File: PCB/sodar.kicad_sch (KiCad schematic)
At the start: 69 parts, among them J1 Conn_02x12_Counter_Clockwise, J2 Screw_Terminal_01x02, U1 TC78H621FNG, U10 TC78H621FNG, U2 TC78H621FNG, U3 TC78H621FNG, U4 TC78H621FNG, U5 TC78H621FNG, U6 TC78H621FNG, U7 TC78H621FNG, U8 TC78H621FNG, U9 TC78H621FNG

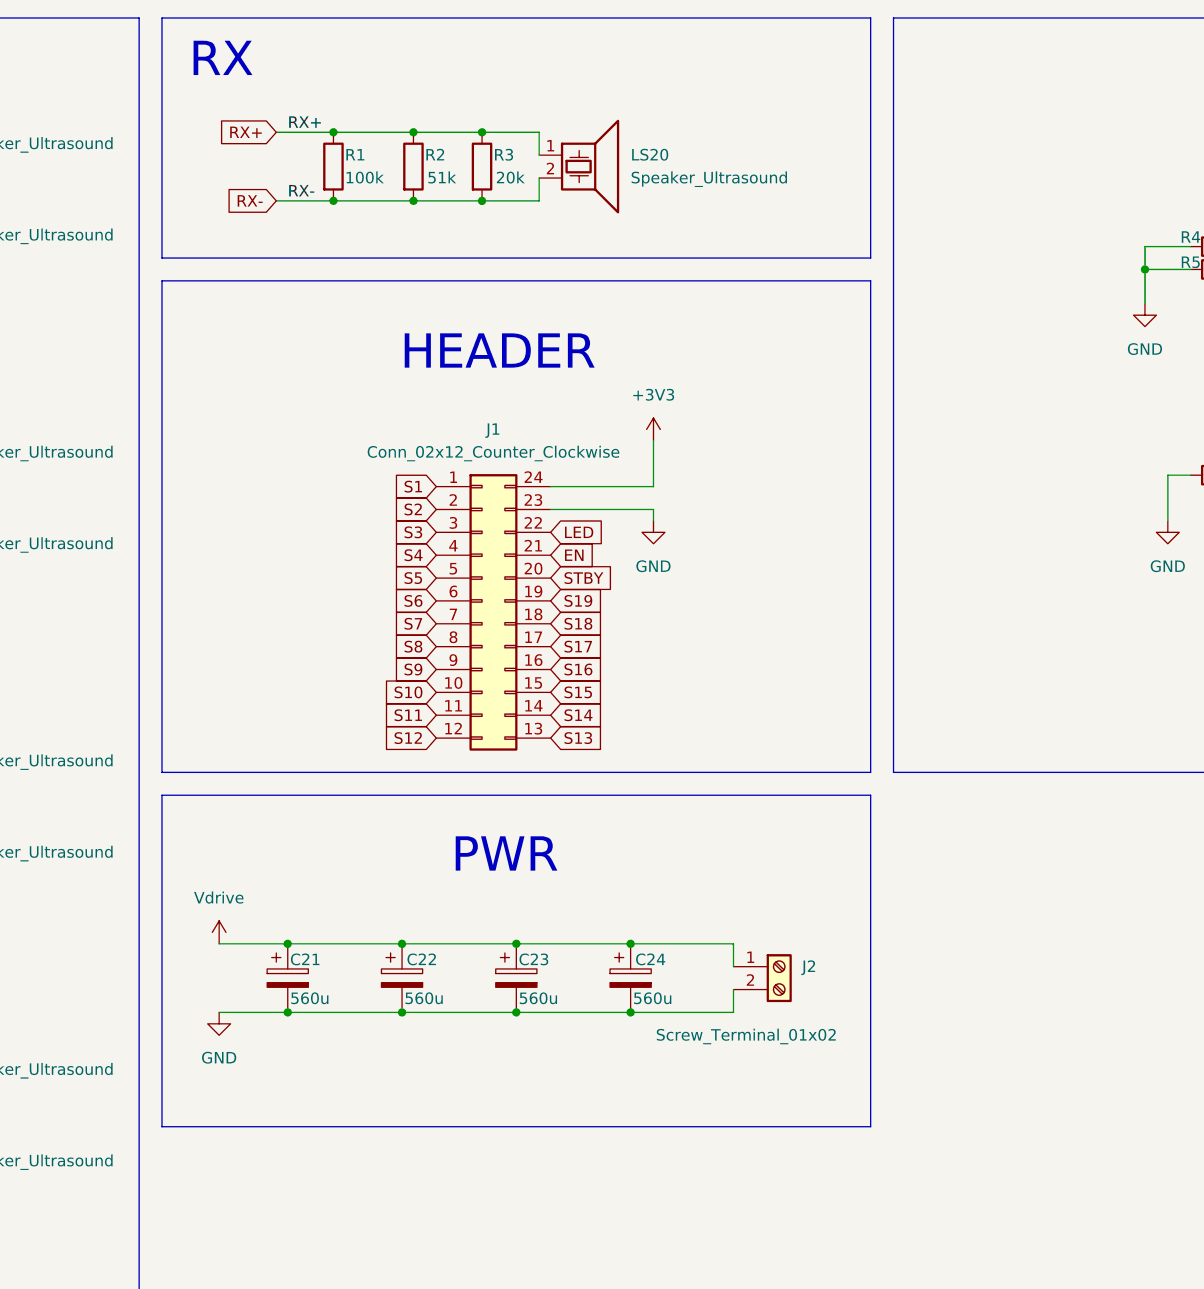
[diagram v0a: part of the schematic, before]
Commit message: Fixed receiver schematics
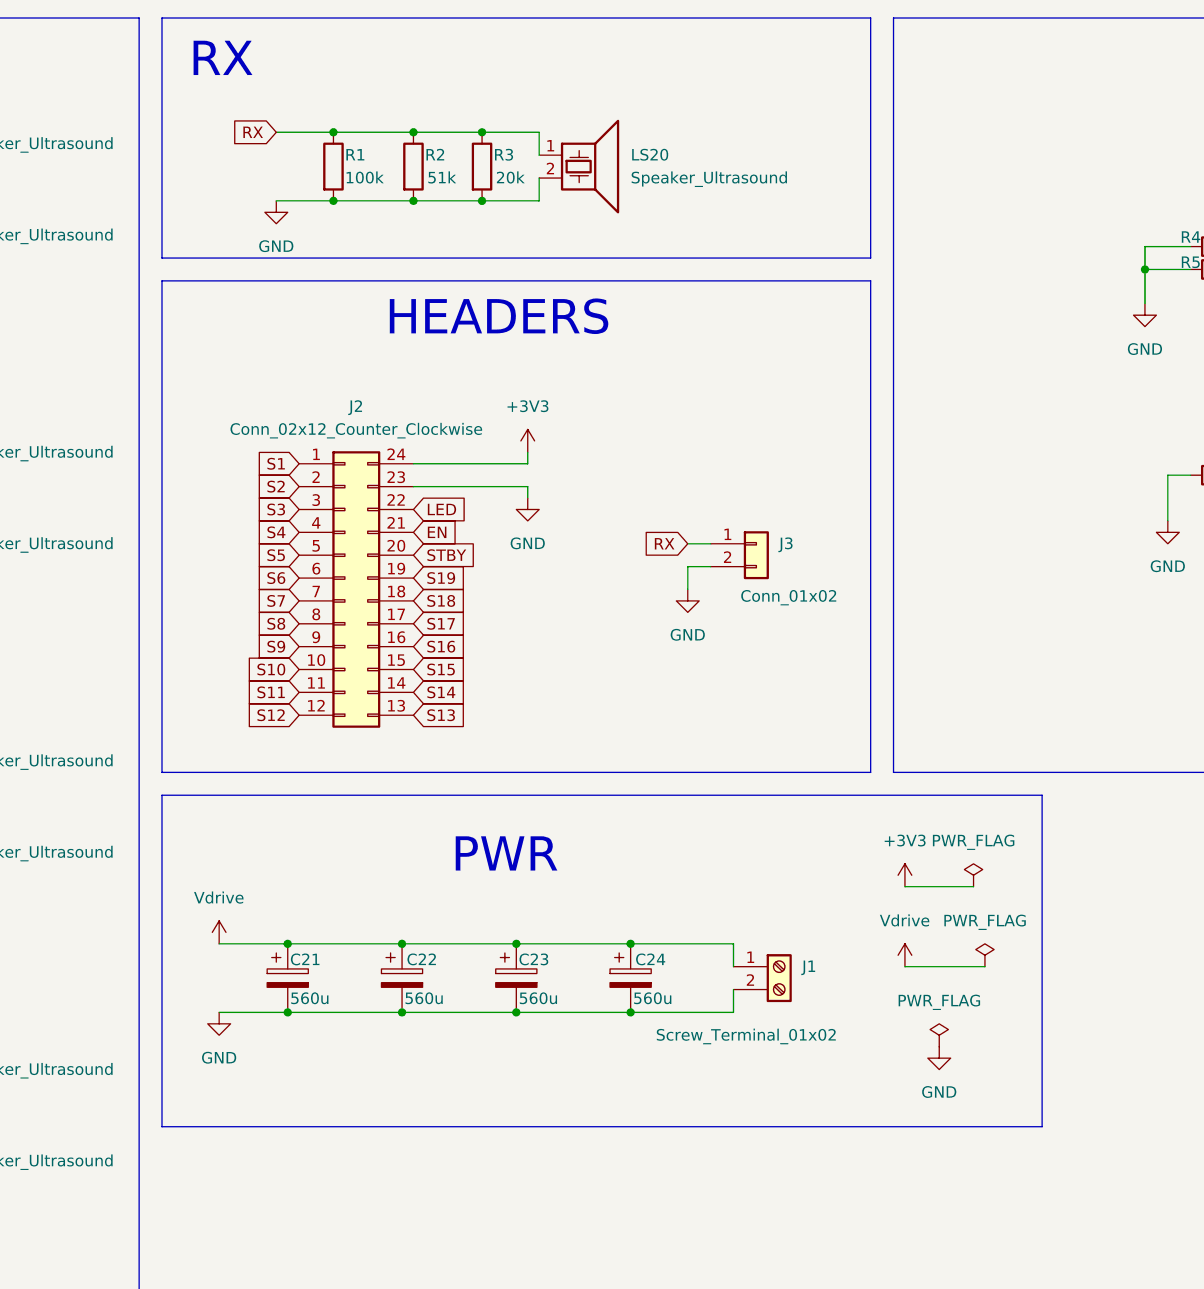
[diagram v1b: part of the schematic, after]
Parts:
- added J3: Conn_01x02, Connector_PinSocket_2.54mm:PinSocket_1x02_P2.54mm_Vertical, symbol Connector_Generic:Conn_01x02
- renumbered J2 to J1, J1 to J2
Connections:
- net RX- is gone; now on net GND: LS20.2, R1.2, R2.2, R3.2
- net GND: now also J3.2 (Pin_2)
- net RX+ renamed RX
- net RX: now also J3.1 (Pin_1)
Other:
- note added: "HEADERS"
- note removed: "HEADER"
- moved on the sheet: J2

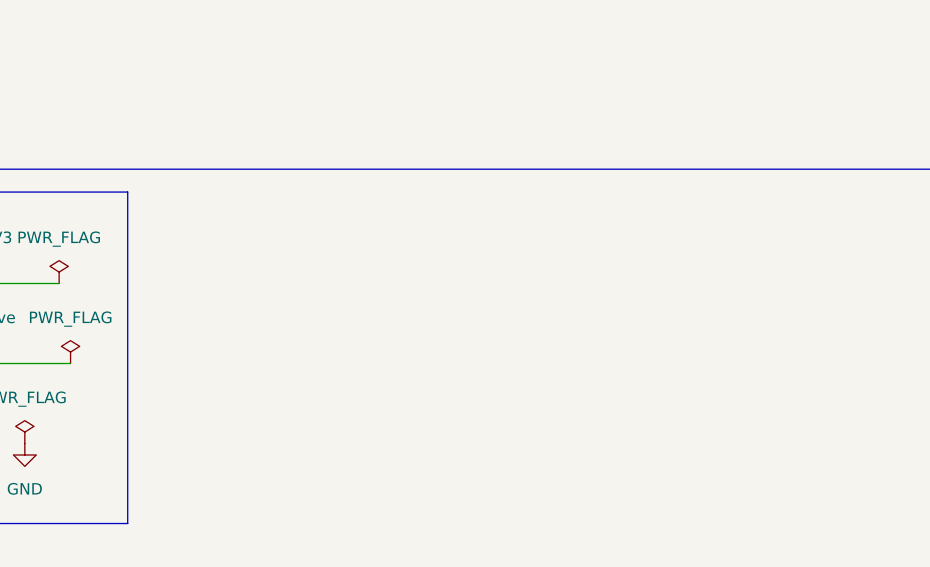
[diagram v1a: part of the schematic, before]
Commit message: Added mounting holes
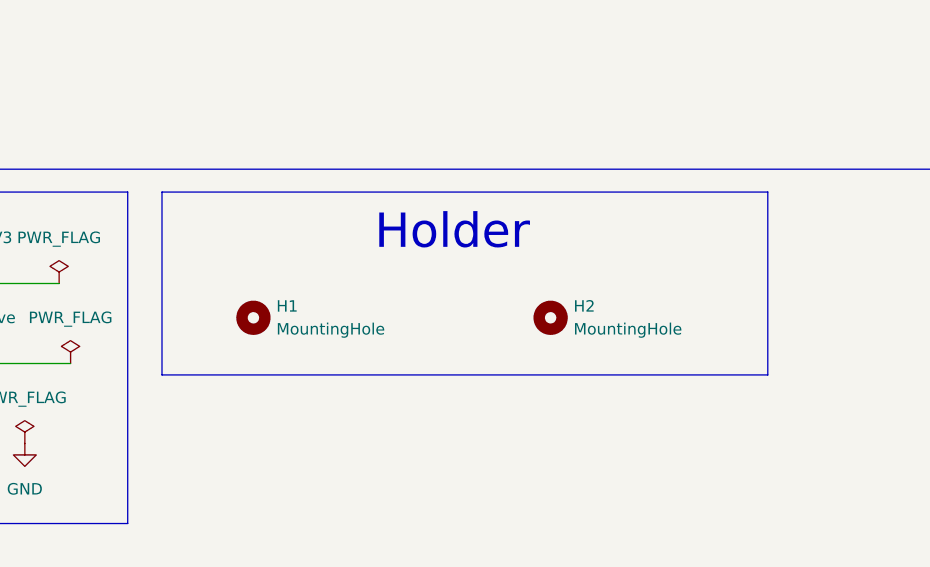
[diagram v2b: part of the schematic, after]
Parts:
- added H1, H2: MountingHole, symbol Mechanical:MountingHole
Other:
- note added: "Holder"
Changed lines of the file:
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@@
 	)
 	(rectangle
+		(start 278.13 100.33)
+		(end 345.44 120.65)
+		(stroke
+			(width 0)
+			(type default)
+		)
+		(fill
+			(type none)
+		)
+	)
+	(rectangle
 		(start 13.97 13.97)
 		(end 173.99 191.77)
@@
 		)
 	)
+	(text "Holder\n"
+		(exclude_from_sim no)
+		(at 310.388 104.902 0)
+		(effects
+			(font
+				(size 3.81 3.81)
+			)
+		)
+	)
 	(junction
 		(at 19.05 44.45)
@@
 	)
 	(symbol
+		(lib_id "Mechanical:MountingHole")
+		(at 321.31 114.3 0)
+		(unit 1)
+		(exclude_from_sim no)
+		(in_bom no)
+		(on_board yes)
+		(dnp no)
+		(fields_autoplaced yes)
+		(property "Reference" "H2"
+			(at 323.85 113.0299 0)
+			(effects
+				(font
+					(size 1.27 1.27)
+				)
+				(justify left)
+			)
+		)
+		(property "Value" "MountingHole"
+			(at 323.85 115.5699 0)
+			(effects
+				(font
+					(size 1.27 1.27)
+				)
+				(justify left)
+			)
+		)
+		(property "Footprint" ""
+			(at 321.31 114.3 0)
+			(effects
+				(font
+					(size 1.27 1.27)
+				)
+				(hide yes)
+			)
+		)
+		(property "Datasheet" "~"
+			(at 321.31 114.3 0)
+			(effects
+				(font
+					(size 1.27 1.27)
+				)
+				(hide yes)
+			)
+		)
+		(property "Description" "Mounting Hole without connection"
+			(at 321.31 114.3 0)
+			(effects
+				(font
+					(size 1.27 1.27)
+				)
+				(hide yes)
+			)
+		)
+		(instances
+			(project ""
+				(path "/f620949f-55f1-4ffa-a6f4-2a6276be8919"
+					(reference "H2")
+					(unit 1)
+				)
+			)
+		)
+	)
+	(symbol
 		(lib_id "Device:C_Polarized")
 		(at 215.9 120.65 0)
@@
 					(unit 1)
 				)
+			)
+		)
+	)
+	(symbol
+		(lib_id "Mechanical:MountingHole")
+		(at 288.29 114.3 0)
+		(unit 1)
+		(exclude_from_sim no)
+		(in_bom no)
+		(on_board yes)
+		(dnp no)
+		(fields_autoplaced yes)
+		(property "Reference" "H1"
+			(at 290.83 113.0299 0)
+			(effects
+				(font
+					(size 1.27 1.27)
+				)
+				(justify left)
+			)
+		)
+		(property "Value" "MountingHole"
+			(at 290.83 115.5699 0)
+			(effects
+				(font
+					(size 1.27 1.27)
+				)
+				(justify left)
+			)
+		)
+		(property "Footprint" ""
+			(at 288.29 114.3 0)
+			(effects
+				(font
+					(size 1.27 1.27)
+				)
+				(hide yes)
+			)
+		)
+		(property "Datasheet" "~"
+			(at 288.29 114.3 0)
+			(effects
+				(font
+					(size 1.27 1.27)
+				)
+				(hide yes)
+			)
+		)
+		(property "Description" "Mounting Hole without connection"
+			(at 288.29 114.3 0)
+			(effects
+				(font
+					(size 1.27 1.27)
+				)
+				(hide yes)
+			)
+		)
+		(instances
+			(project ""
+				(path "/f620949f-55f1-4ffa-a6f4-2a6276be8919"
+					(reference "H1")
+					(unit 1)
+				)

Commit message: connected all and fixed all of the errors
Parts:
- H1, H2: footprint (none) -> MountingHole:MountingHole_3.2mm_M3
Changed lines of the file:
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@@
 			)
 		)
-		(property "Footprint" ""
+		(property "Footprint" "MountingHole:MountingHole_3.2mm_M3"
 			(at 321.31 114.3 0)
 			(effects
@@
 			)
 		)
-		(property "Footprint" ""
+		(property "Footprint" "MountingHole:MountingHole_3.2mm_M3"
 			(at 288.29 114.3 0)
 			(effects

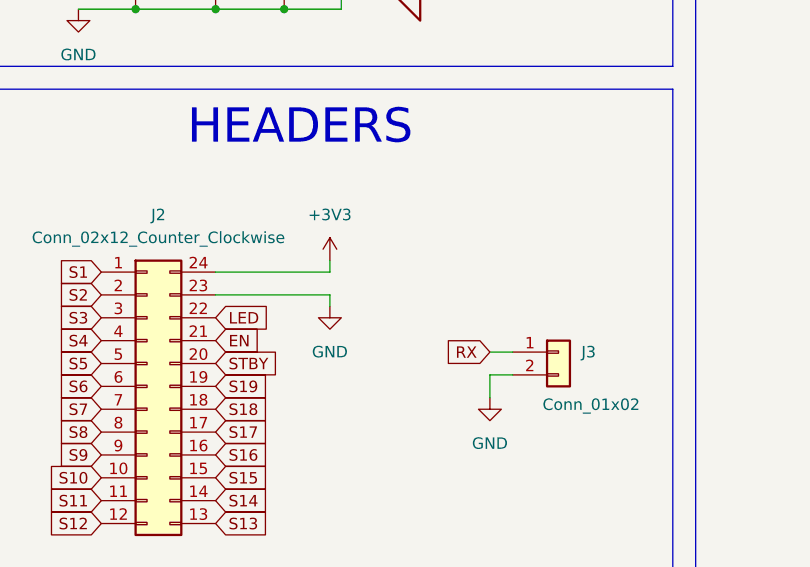
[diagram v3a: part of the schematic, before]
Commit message: Added cap on 3.3V and changed the place for a vdrive and rerouted nececery things
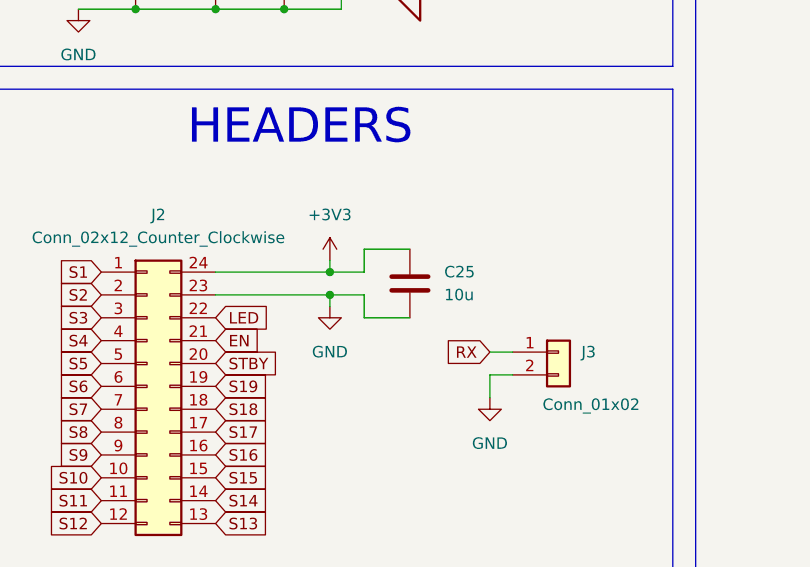
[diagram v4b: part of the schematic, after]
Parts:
- added C25: 10u, Capacitor_SMD:C_0805_2012Metric, symbol Device:C
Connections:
- net +3V3: now also C25.1
- net GND: now also C25.2
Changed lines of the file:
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@@
 	)
 	(junction
+		(at 217.17 63.5)
+		(diameter 0)
+		(color 0 0 0 0)
+	)
+	(junction
 		(at 135.89 147.32)
 		(diameter 0)
@@
 	)
 	(junction
+		(at 217.17 66.04)
+		(diameter 0)
+		(color 0 0 0 0)
+	)
+	(junction
 		(at 104.14 101.6)
 		(diameter 0)
@@
 	(wire
 		(pts
+			(xy 220.98 60.96) (xy 226.06 60.96)
+		)
+		(stroke
+			(width 0)
+			(type default)
+		)
+	)
+	(wire
+		(pts
 			(xy 143.51 33.02) (xy 143.51 35.56)
 		)
@@
 	(wire
 		(pts
+			(xy 217.17 66.04) (xy 220.98 66.04)
+		)
+		(stroke
+			(width 0)
+			(type default)
+		)
+	)
+	(wire
+		(pts
 			(xy 215.9 124.46) (xy 228.6 124.46)
 		)
@@
 	(wire
 		(pts
+			(xy 226.06 68.58) (xy 220.98 68.58)
+		)
+		(stroke
+			(width 0)
+			(type default)
+		)
+	)
+	(wire
+		(pts
 			(xy 19.05 134.62) (xy 19.05 135.89)
 		)
@@
 	(wire
 		(pts
+			(xy 220.98 68.58) (xy 220.98 66.04)
+		)
+		(stroke
+			(width 0)
+			(type default)
+		)
+	)
+	(wire
+		(pts
 			(xy 135.89 57.15) (xy 140.97 57.15)
 		)
@@
 	(wire
 		(pts
+			(xy 217.17 63.5) (xy 220.98 63.5)
+		)
+		(stroke
+			(width 0)
+			(type default)
+		)
+	)
+	(wire
+		(pts
 			(xy 212.09 34.29) (xy 218.44 34.29)
 		)
@@
 	(wire
 		(pts
+			(xy 220.98 63.5) (xy 220.98 60.96)
+		)
+		(stroke
+			(width 0)
+			(type default)
+		)
+	)
+	(wire
+		(pts
 			(xy 290.83 41.91) (xy 285.75 41.91)
 		)
@@
 					(unit 1)
 				)
+			)
+		)
+	)
+	(symbol
+		(lib_id "Device:C")
+		(at 226.06 64.77 0)
+		(unit 1)
+		(exclude_from_sim no)
+		(in_bom yes)
+		(on_board yes)
+		(dnp no)
+		(fields_autoplaced yes)
+		(property "Reference" "C25"
+			(at 229.87 63.4999 0)
+			(effects
+				(font
+					(size 1.27 1.27)
+				)
+				(justify left)
+			)
+		)
+		(property "Value" "10u"
+			(at 229.87 66.0399 0)
+			(effects
+				(font
+					(size 1.27 1.27)
+				)
+				(justify left)
+			)
+		)
+		(property "Footprint" "Capacitor_SMD:C_0805_2012Metric"
+			(at 227.0252 68.58 0)
+			(effects
+				(font
+					(size 1.27 1.27)
+				)
+				(hide yes)
+			)
+		)
+		(property "Datasheet" "~"
+			(at 226.06 64.77 0)
+			(effects
+				(font
+					(size 1.27 1.27)
+				)
+				(hide yes)
+			)
+		)
+		(property "Description" "Unpolarized capacitor"
+			(at 226.06 64.77 0)
+			(effects
+				(font
+					(size 1.27 1.27)
+				)
+				(hide yes)
+			)
+		)
+		(pin "2"
+		)
+		(pin "1"
+		)
+		(instances
+			(project ""
+				(path "/f620949f-55f1-4ffa-a6f4-2a6276be8919"
+					(reference "C25")
+					(unit 1)
+				)
